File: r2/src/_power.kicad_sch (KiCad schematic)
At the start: 24 parts, among them J1 532610271, Q4 DMG2305UX-13, Q5 DMG2305UX-13, U1 MCP73831T-2ACI_OT, U2 AP2114H-3_3TRG1

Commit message: Correct switch symbol so default switch behaviour from factory is correctly shown.
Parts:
- S3: symbol j_Switch:JS102011SAQN -> j_Switch:K3-1296S; MPN K3-1296S-J1 -> K3-1296S
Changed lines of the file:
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@@
   (junction (at 151.13 88.9) (diameter 0) (color 0 0 0 0)
   )
-  (no_connect (at 166.37 132.08))
+  (no_connect (at 161.29 132.08))
   (wire (pts (xy 163.83 57.15) (xy 186.69 57.15))
     (stroke (width 0) (type default))
@@
     (stroke (width 0) (type default))
   )
-  (wire (pts (xy 161.29 132.08) (xy 161.29 138.43))
+  (wire (pts (xy 166.37 132.08) (xy 166.37 138.43))
     (stroke (width 0) (type default))
   )
@@
     )
   )
-  (symbol (lib_id "power:GND") (at 161.29 138.43 0) (mirror y) (unit 1)
-    (in_bom yes) (on_board yes) (dnp no)
-    (property "Reference" "#PWR017" (at 161.29 144.78 0)
-      (effects (font (size 1.27 1.27)) hide)
-    )
-    (property "Value" "GND" (at 161.163 142.8242 0)
+  (symbol (lib_id "power:GND") (at 166.37 138.43 0) (mirror y) (unit 1)
+    (in_bom yes) (on_board yes) (dnp no)
+    (property "Reference" "#PWR017" (at 166.37 144.78 0)
+      (effects (font (size 1.27 1.27)) hide)
+    )
+    (property "Value" "GND" (at 166.243 142.8242 0)
       (effects (font (size 1.27 1.27)))
     )
-    (property "Footprint" "" (at 161.29 138.43 0)
-      (effects (font (size 1.27 1.27)) hide)
-    )
-    (property "Datasheet" "" (at 161.29 138.43 0)
+    (property "Footprint" "" (at 166.37 138.43 0)
+      (effects (font (size 1.27 1.27)) hide)
+    )
+    (property "Datasheet" "" (at 166.37 138.43 0)
       (effects (font (size 1.27 1.27)) hide)
     )
@@
     )
   )
-  (symbol (lib_id "j_Switch:JS102011SAQN") (at 163.83 124.46 90) (unit 1)
+  (symbol (lib_id "j_Switch:K3-1296S") (at 163.83 124.46 90) (unit 1)
     (in_bom yes) (on_board yes) (dnp no)
     (property "Reference" "S3" (at 168.3258 123.2916 90)
@@
       (effects (font (size 1.27 1.27)) (justify left bottom) hide)
     )
-    (property "MPN" "K3-1296S-J1" (at 163.83 124.46 90)
-      (effects (font (size 1.27 1.27)) hide)
+    (property "MPN" "K3-1296S" (at 163.83 124.46 0)
+      (effects (font (size 1.27 1.27)) (justify left bottom) hide)
     )
     (property "LCSC" "C223848" (at 163.83 124.46 90)
       (effects (font (size 1.27 1.27)) hide)
     )
-    (property "Manufacturer" "HRO" (at 163.83 124.46 90)
-      (effects (font (size 1.27 1.27)) hide)
-    )
-    (pin "1")
-    (pin "2")
+    (property "Manufacturer" "HRO" (at 163.83 124.46 0)
+      (effects (font (size 1.27 1.27)) (justify left bottom) hide)
+    )
+    (pin "2")
+    (pin "1")
     (pin "3")
     (instances

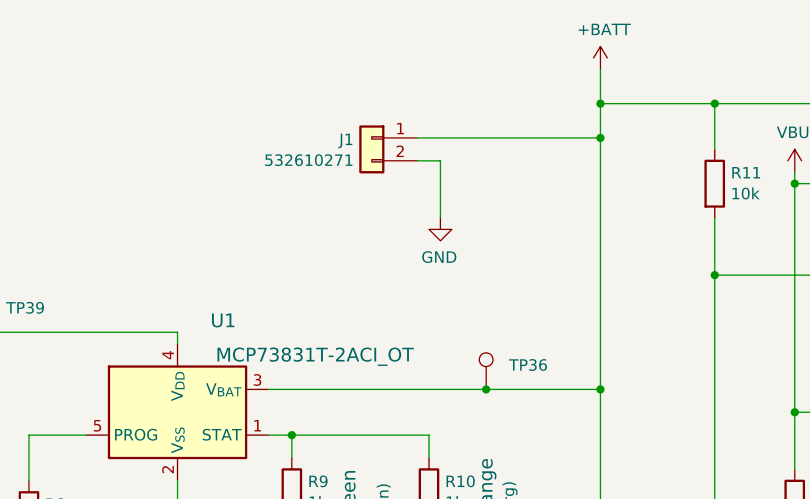
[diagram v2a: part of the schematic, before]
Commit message: Change battery connector symbol to include mounting pads.
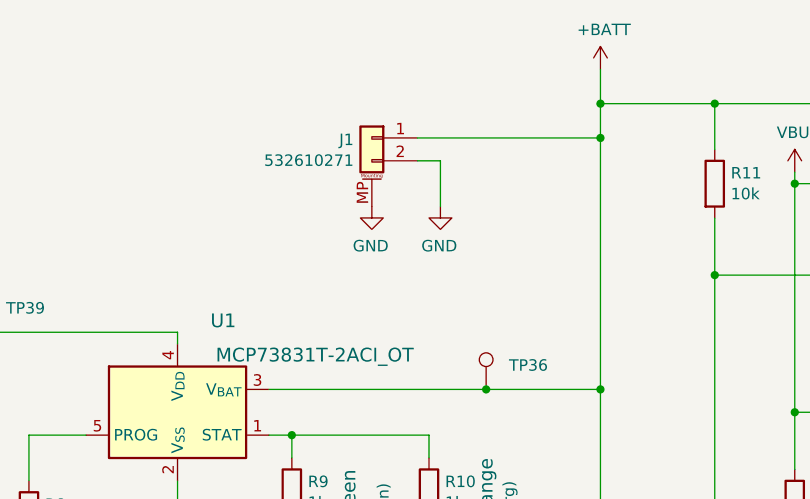
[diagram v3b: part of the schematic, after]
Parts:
- J1: symbol Connector_Generic:Conn_01x02 -> Connector_Generic_MountingPin:Conn_01x02_MountingPin
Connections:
- net GND: now also J1.MP (MountPin)
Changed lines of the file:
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@@
     (stroke (width 0) (type default))
   )
-  (wire (pts (xy 133.35 63.5) (xy 133.35 69.85))
+  (wire (pts (xy 133.35 63.5) (xy 133.35 68.58))
     (stroke (width 0) (type default))
   )
@@
     )
   )
-  (symbol (lib_id "Connector_Generic:Conn_01x02") (at 125.73 60.96 0) (mirror y) (unit 1)
+  (symbol (lib_id "Connector_Generic_MountingPin:Conn_01x02_MountingPin") (at 125.73 60.96 0) (mirror y) (unit 1)
     (in_bom yes) (on_board yes) (dnp no)
     (property "Reference" "J1" (at 123.7234 61.1632 0)
@@
     (pin "1")
     (pin "2")
+    (pin "MP")
     (instances
       (project "tr23-badge-r2"
@@
     )
   )
-  (symbol (lib_id "power:GND") (at 133.35 69.85 0) (mirror y) (unit 1)
-    (in_bom yes) (on_board yes) (dnp no)
-    (property "Reference" "#PWR015" (at 133.35 76.2 0)
-      (effects (font (size 1.27 1.27)) hide)
-    )
-    (property "Value" "GND" (at 133.223 74.2442 0)
-      (effects (font (size 1.27 1.27)))
-    )
-    (property "Footprint" "" (at 133.35 69.85 0)
-      (effects (font (size 1.27 1.27)) hide)
-    )
-    (property "Datasheet" "" (at 133.35 69.85 0)
+  (symbol (lib_id "power:GND") (at 133.35 68.58 0) (mirror y) (unit 1)
+    (in_bom yes) (on_board yes) (dnp no)
+    (property "Reference" "#PWR015" (at 133.35 74.93 0)
+      (effects (font (size 1.27 1.27)) hide)
+    )
+    (property "Value" "GND" (at 133.223 72.9742 0)
+      (effects (font (size 1.27 1.27)))
+    )
+    (property "Footprint" "" (at 133.35 68.58 0)
+      (effects (font (size 1.27 1.27)) hide)
+    )
+    (property "Datasheet" "" (at 133.35 68.58 0)
       (effects (font (size 1.27 1.27)) hide)
     )
@@
         )
       )
+    )
+  )
+  (symbol (lib_id "power:GND") (at 125.73 68.58 0) (mirror y) (unit 1)
+    (in_bom yes) (on_board yes) (dnp no)
+    (property "Reference" "#PWR0156" (at 125.73 74.93 0)
+      (effects (font (size 1.27 1.27)) hide)
+    )
+    (property "Value" "GND" (at 125.603 72.9742 0)
+      (effects (font (size 1.27 1.27)))
+    )
+    (property "Footprint" "" (at 125.73 68.58 0)
+      (effects (font (size 1.27 1.27)) hide)
+    )
+    (property "Datasheet" "" (at 125.73 68.58 0)
+      (effects (font (size 1.27 1.27)) hide)
+    )
+    (pin "1")
+    (instances
+      (project "tr23-badge-r2"
+        (path "/ab725fe7-4504-40ef-b6af-82d065d00fb6/00000000-0000-0000-0000-00005ddaba4a"
+          (reference "#PWR0156") (unit 1)
+        )
+        (path "/ab725fe7-4504-40ef-b6af-82d065d00fb6"
+          (reference "#PWR?") (unit 1)
+        )
+      )

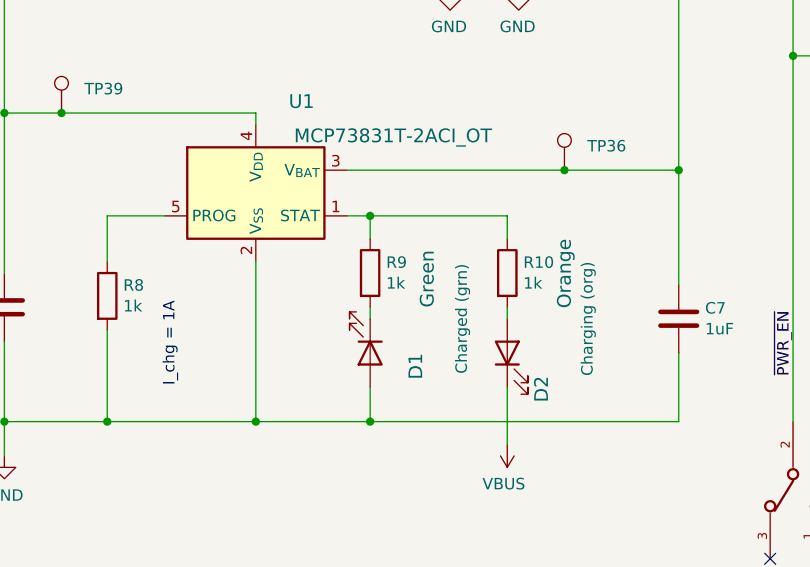
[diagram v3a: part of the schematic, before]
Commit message: Increase resistance of charging LED resistor - it was extremely bright
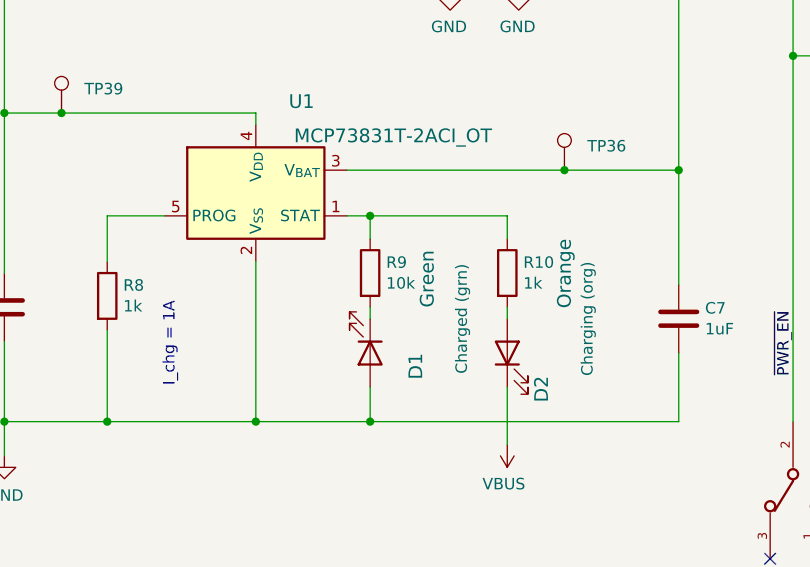
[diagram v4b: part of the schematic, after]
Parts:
- R9: value 1k -> 10k
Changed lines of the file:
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@@
       (effects (font (size 1.27 1.27)) (justify left))
     )
-    (property "Value" "1k" (at 118.618 101.473 0)
+    (property "Value" "10k" (at 118.618 101.473 0)
       (effects (font (size 1.27 1.27)) (justify left))
     )

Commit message: Set title block contents
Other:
- company: (none) -> Monad Gottfried Ltd. 2023
- title: (none) -> Troopers 23 Badge
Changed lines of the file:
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@@
 (kicad_sch (version 20230409) (generator eeschema)
   (paper "A4")
+  (title_block
+    (title "Troopers 23 Badge")
+    (rev "r2")
+    (company "Monad Gottfried Ltd. 2023")
+    (comment 1 "for ERNW Enno Rey Netzwerke GmbH")
+  )
   (junction (at 87.63 116.84) (diameter 0) (color 0 0 0 0)
   )
